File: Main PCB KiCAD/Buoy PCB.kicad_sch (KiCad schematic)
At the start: 4 parts, among them J1 Conn_01x12_Socket, J2 Conn_01x12_Socket, J3 Conn_01x12_Pin, J4 Conn_01x12_Pin

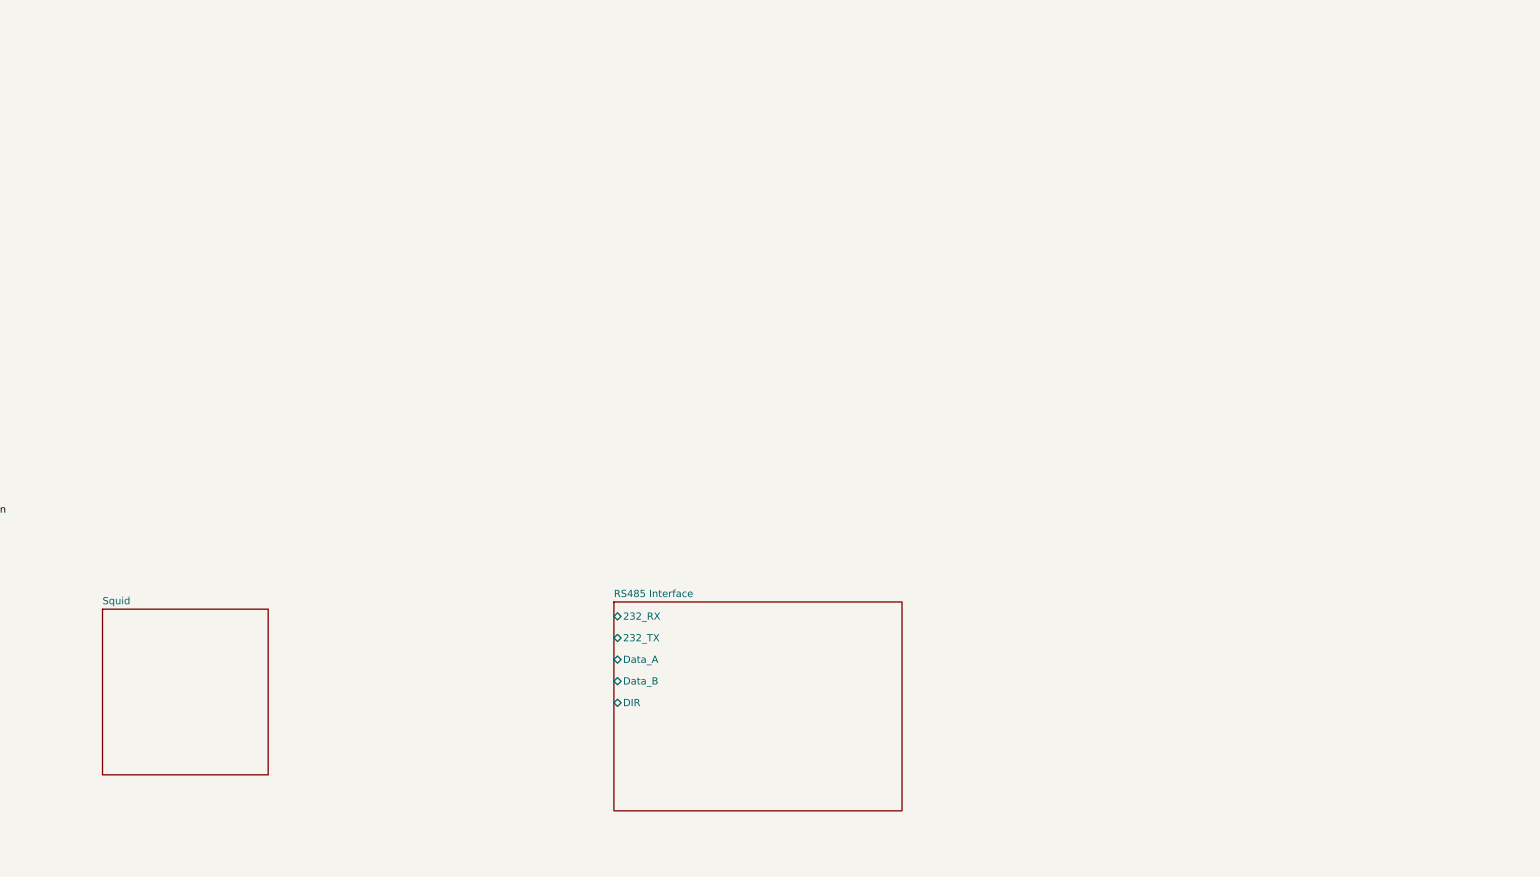
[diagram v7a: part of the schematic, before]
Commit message: removed shrimp and replaced with Arduino Mega 328
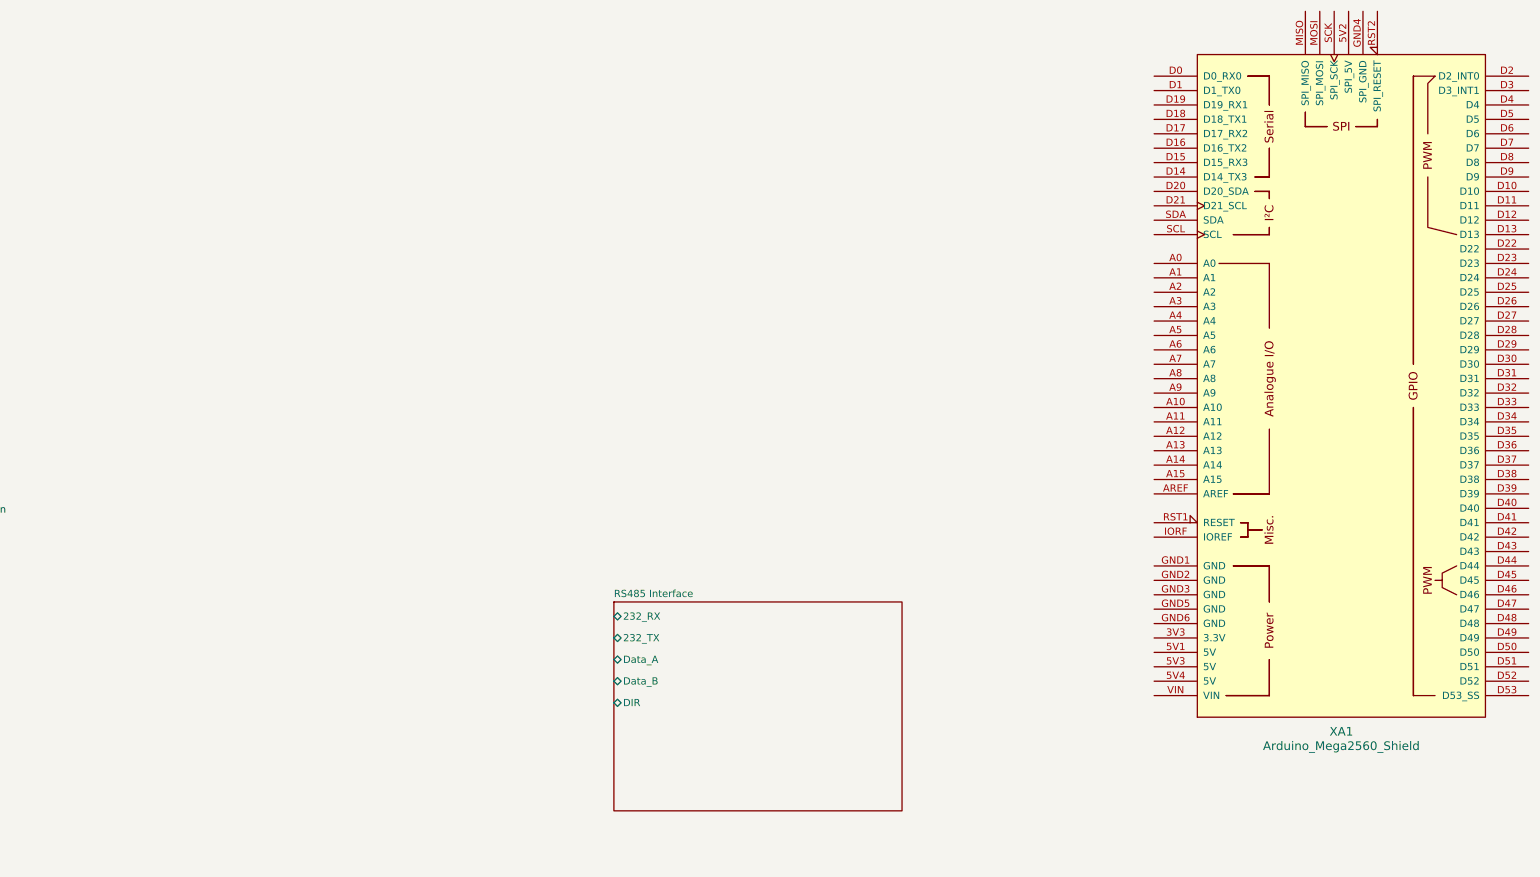
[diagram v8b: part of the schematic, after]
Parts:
- added XA1: Arduino_Mega2560_Shield, Arduino:Arduino_Mega2560_Shield, symbol Arduino:Arduino_Mega2560_Shield
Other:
- removed sheet Squid
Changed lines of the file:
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@@
+	)
+	(symbol
+		(lib_id "Arduino:Arduino_Mega2560_Shield")
+		(at 349.25 0 0)
+		(unit 1)
+		(exclude_from_sim no)
+		(in_bom yes)
+		(on_board yes)
+		(dnp no)
+		(fields_autoplaced yes)
+		(property "Reference" "XA1"
+			(at 349.25 60.96 0)
+			(effects
+				(font
+					(size 1.524 1.524)
+				)
+			)
+		)
+		(property "Value" "Arduino_Mega2560_Shield"
+			(at 349.25 63.5 0)
+			(effects
+				(font
+					(size 1.524 1.524)
+				)
+			)
+		)
+		(property "Footprint" "Arduino:Arduino_Mega2560_Shield"
+			(at 367.03 -69.85 0)
+			(effects
+				(font
+					(size 1.524 1.524)
+				)
+				(hide yes)
+			)
+		)
+		(property "Datasheet" ""
+			(at 367.03 -69.85 0)
+			(effects
+				(font
+					(size 1.524 1.524)
+				)
+				(hide yes)
+			)
+		)
+		(property "Description" ""
+			(at 349.25 0 0)
+			(effects
+				(font
+					(size 1.27 1.27)
+				)
+				(hide yes)
+			)
+		)
+		(pin "D19"
+		)
+		(pin "D1"
+		)
+		(pin "D18"
+		)
+		(pin "D17"
+		)
+		(pin "D16"
+		)
+		(pin "D15"
+		)
+		(pin "D14"
+		)
+		(pin "D20"
+		)
+		(pin "D21"
+		)
+		(pin "SDA"
+		)
+		(pin "SCL"
+		)
+		(pin "A0"
+		)
+		(pin "A1"
+		)
+		(pin "A2"
+		)
+		(pin "A3"
+		)
+		(pin "A4"
+		)
+		(pin "A5"
+		)
+		(pin "A6"
+		)
+		(pin "A7"
+		)
+		(pin "A8"
+		)
+		(pin "A9"
+		)
+		(pin "A10"
+		)
+		(pin "A11"
+		)
+		(pin "A12"
+		)
+		(pin "A13"
+		)
+		(pin "A14"
+		)
+		(pin "A15"
+		)
+		(pin "AREF"
+		)
+		(pin "RST1"
+		)
+		(pin "IORF"
+		)
+		(pin "GND1"
+		)
+		(pin "GND2"
+		)
+		(pin "GND3"
+		)
+		(pin "GND5"
+		)
+		(pin "GND6"
+		)
+		(pin "3V3"
+		)
+		(pin "5V1"
+		)
+		(pin "5V3"
+		)
+		(pin "5V4"
+		)
+		(pin "VIN"
+		)
+		(pin "MISO"
+		)
+		(pin "MOSI"
+		)
+		(pin "SCK"
+		)
+		(pin "5V2"
+		)
+		(pin "GND4"
+		)
+		(pin "RST2"
+		)
+		(pin "D2"
+		)
+		(pin "D3"
+		)
+		(pin "D4"
+		)
+		(pin "D5"
+		)
+		(pin "D6"
+		)
+		(pin "D7"
+		)
+		(pin "D8"
+		)
+		(pin "D9"
+		)
+		(pin "D10"
+		)
+		(pin "D11"
+		)
+		(pin "D12"
+		)
+		(pin "D13"
+		)
+		(pin "D22"
+		)
+		(pin "D23"
+		)
+		(pin "D24"
+		)
+		(pin "D25"
+		)
+		(pin "D26"
+		)
+		(pin "D27"
+		)
+		(pin "D28"
+		)
+		(pin "D29"
+		)
+		(pin "D30"
+		)
+		(pin "D31"
+		)
+		(pin "D32"
+		)
+		(pin "D33"
+		)
+		(pin "D34"
+		)
+		(pin "D35"
+		)
+		(pin "D36"
+		)
+		(pin "D37"
+		)
+		(pin "D38"
+		)
+		(pin "D39"
+		)
+		(pin "D40"
+		)
+		(pin "D41"
+		)
+		(pin "D42"
+		)
+		(pin "D43"
+		)
+		(pin "D44"
+		)
+		(pin "D45"
+		)
+		(pin "D46"
+		)
+		(pin "D47"
+		)
+		(pin "D48"
+		)
+		(pin "D49"
+		)
+		(pin "D50"
+		)
+		(pin "D51"
+		)
+		(pin "D52"
+		)
+		(pin "D53"
+		)
+		(pin "D0"
+		)
+		(instances
+			(project ""
+				(path "/a041e2a6-7d41-458c-91f3-753821d3dfe9"
+					(reference "XA1")
+					(unit 1)
+				)
+			)
+		)
 	)
 	(symbol
@@
 				)
 			)
-		)
-	)
-	(sheet
-		(at 130.81 39.37)
-		(size 29.21 29.21)
-		(exclude_from_sim no)
-		(in_bom yes)
-		(on_board yes)
-		(dnp no)
-		(fields_autoplaced yes)
-		(stroke
-			(width 0.1524)
-			(type solid)
-		)
-		(fill
-			(color 0 0 0 0.0000)
-		)
-		(property "Sheetname" "Squid"
-			(at 130.81 38.6584 0)
-			(effects
-				(font
-					(size 1.27 1.27)
-				)
-				(justify left bottom)
-			)
-		)
-		(property "Sheetfile" "Assets/SubPCBs/Shrimps/Shrimp ATmega328P-P.kicad_sch"
-			(at 130.81 69.1646 0)
-			(effects
-				(font
-					(size 1.27 1.27)
-				)
-				(justify left top)
-				(hide yes)
-			)
-		)
-		(instances
-			(project "Buoy PCB"
-				(path "/a041e2a6-7d41-458c-91f3-753821d3dfe9"
-					(page "2")
-				)
-			)
